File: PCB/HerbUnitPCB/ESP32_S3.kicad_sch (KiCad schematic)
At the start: 26 parts, among them J1 USB_C_Receptacle_USB2.0_16P, J2 Barrel_Jack_Switch_Pin3Ring, SW1 SW_Push, SW2 SW_Push, U1 USBLC6-2P6, U2 ESP32-S3-WROOM-1, U3 AMS1117-5.0, U4 AP2112K-3.3

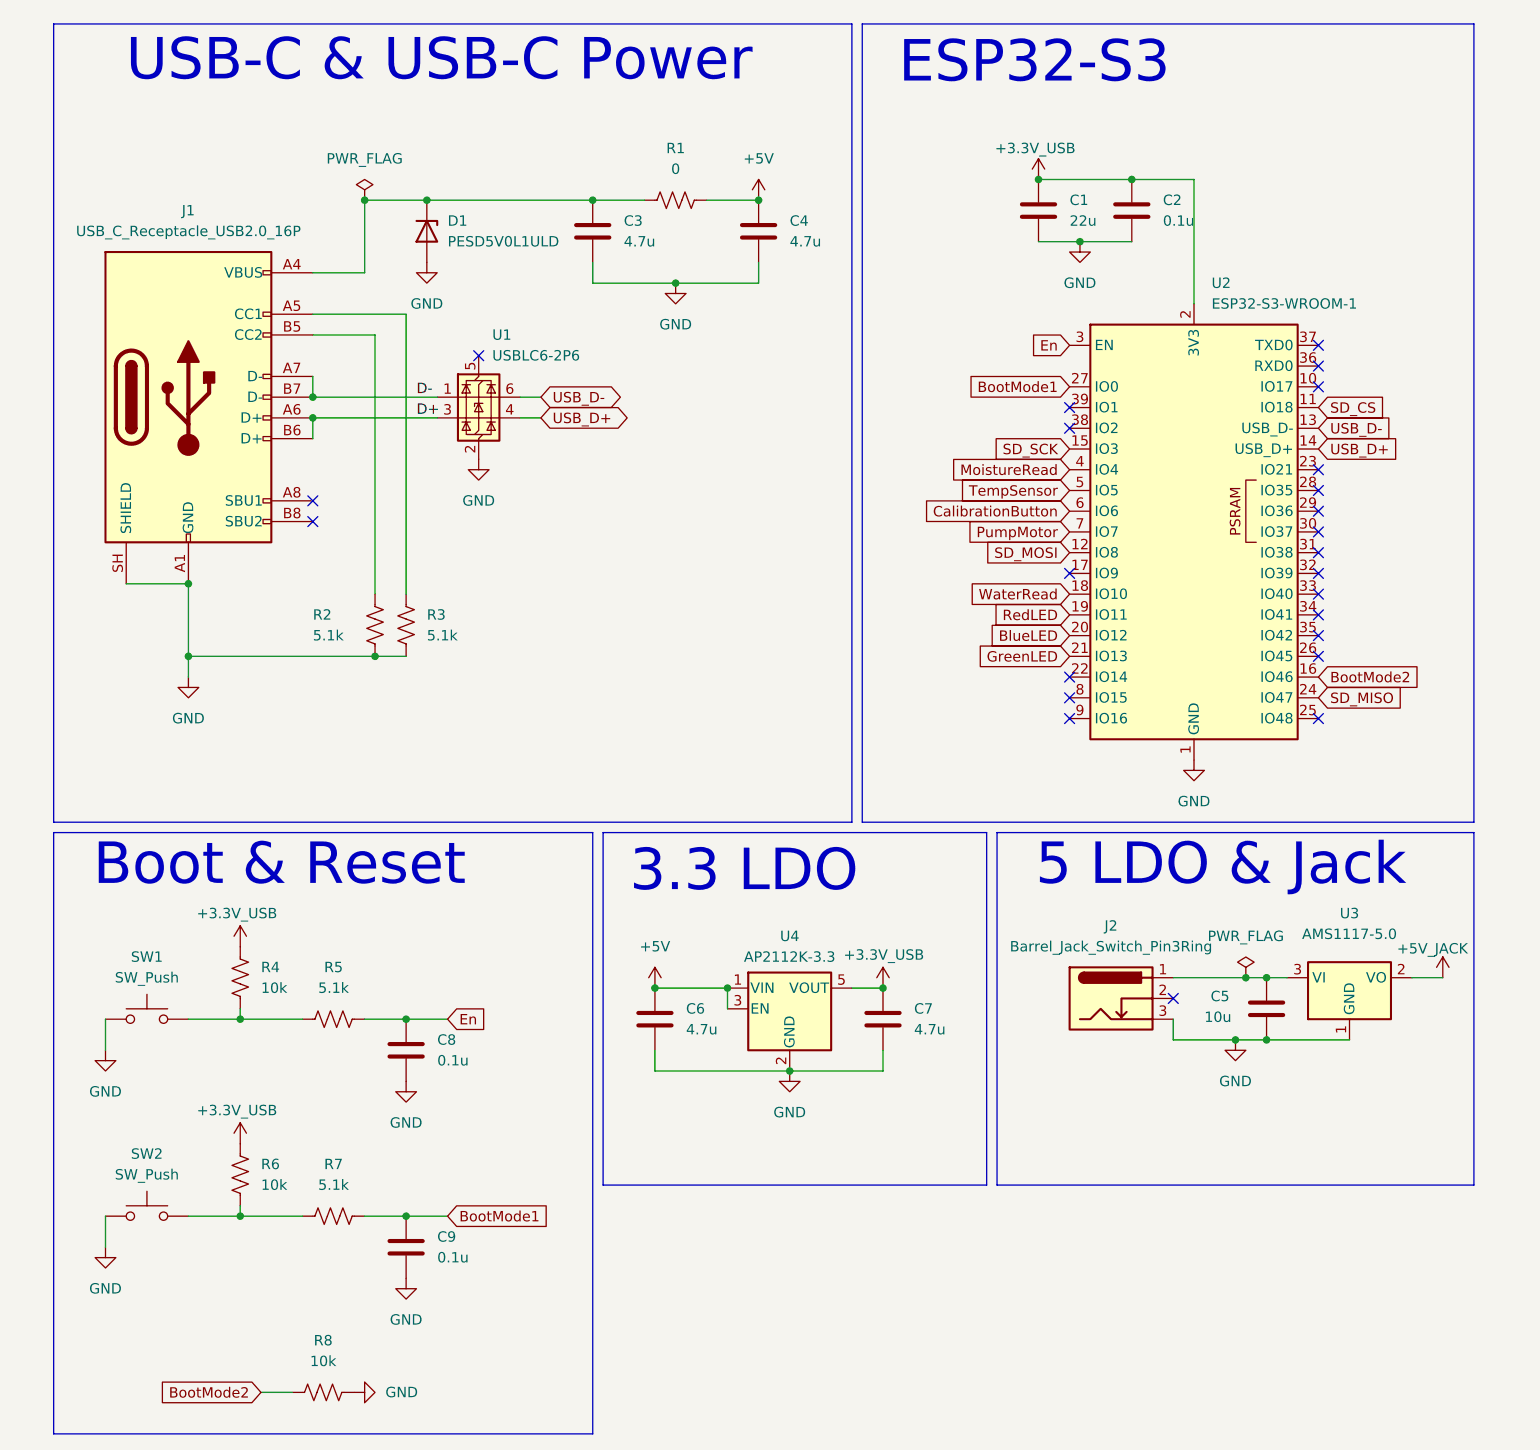
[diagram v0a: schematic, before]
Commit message: Started PCB design
- Assigned footprints to remaining components
- Brought components into PCB editor and laid them out in general groups
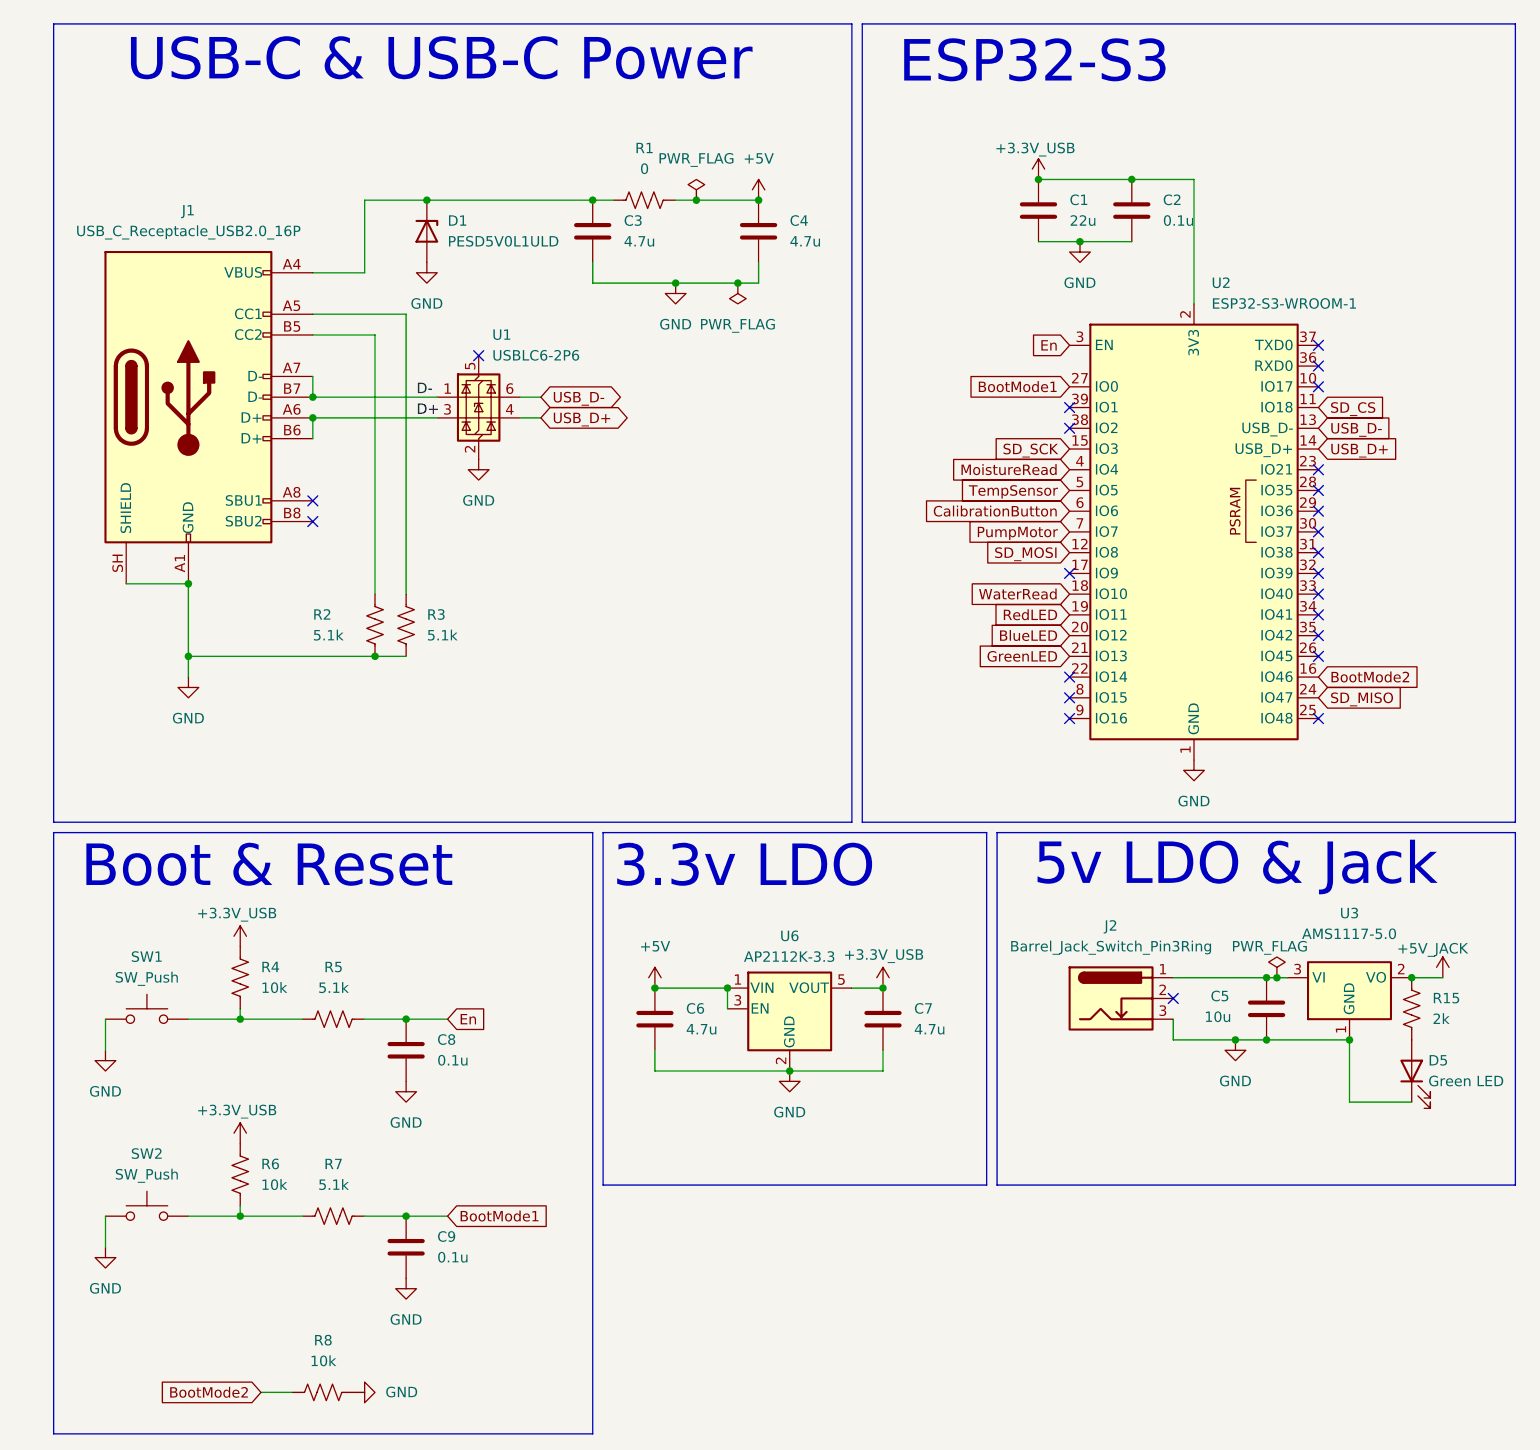
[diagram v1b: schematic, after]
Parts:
- removed U4: AP2112K-3.3, Package_TO_SOT_SMD:SOT-23-5, symbol Regulator_Linear:AP2112K-3.3
- added D5: Green LED, LED_SMD:LED_0201_0603Metric, symbol Device:LED
- added R15: 2k, Resistor_SMD:R_0402_1005Metric, symbol Device:R_US
- added U6: AP2112K-3.3, Package_TO_SOT_SMD:SOT-23-5, symbol Regulator_Linear:AP2112K-3.3
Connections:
- net +3.3V_USB: now also U6.5 (VOUT)
- net +5V: now also U6.1 (VIN), U6.3 (EN)
- net +5V_JACK: now also R15.1
- net GND: now also D5.1 (K), U6.2 (GND)
- new net: D5.2 (A), R15.2
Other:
- note added: "3.3v LDO"
- note added: "5v LDO & Jack"
- note removed: "3.3 LDO"
- note removed: "5 LDO & Jack"
- moved on the sheet: R1

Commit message: Arranged components
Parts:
- C1, C3, C4, C5, C6, C7: footprint Capacitor_SMD:C_0402_1005Metric -> Capacitor_SMD:C_0805_2012Metric
- R1: footprint (none) -> Resistor_SMD:R_0805_2012Metric
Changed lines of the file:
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@@
 			)
 		)
-		(property "Footprint" "Capacitor_SMD:C_0402_1005Metric"
+		(property "Footprint" "Capacitor_SMD:C_0805_2012Metric"
 			(at 116.5352 139.7 0)
 			(hide yes)
@@
 			)
 		)
-		(property "Footprint" "Capacitor_SMD:C_0402_1005Metric"
+		(property "Footprint" "Capacitor_SMD:C_0805_2012Metric"
 			(at 80.9752 43.18 0)
 			(hide yes)
@@
 			)
 		)
-		(property "Footprint" "Capacitor_SMD:C_0402_1005Metric"
+		(property "Footprint" "Capacitor_SMD:C_0805_2012Metric"
 			(at 88.5952 139.7 0)
 			(hide yes)
@@
 			)
 		)
-		(property "Footprint" "Capacitor_SMD:C_0402_1005Metric"
+		(property "Footprint" "Capacitor_SMD:C_0805_2012Metric"
 			(at 163.5252 138.43 0)
 			(hide yes)
@@
 			)
 		)
-		(property "Footprint" ""
+		(property "Footprint" "Resistor_SMD:R_0805_2012Metric"
 			(at 86.614 34.544 90)
 			(hide yes)
@@
 			)
 		)
-		(property "Footprint" "Capacitor_SMD:C_0402_1005Metric"
+		(property "Footprint" "Capacitor_SMD:C_0805_2012Metric"
 			(at 101.2952 43.18 0)
 			(hide yes)
@@
 			)
 		)
-		(property "Footprint" "Capacitor_SMD:C_0402_1005Metric"
+		(property "Footprint" "Capacitor_SMD:C_0805_2012Metric"
 			(at 135.5852 40.64 0)
 			(hide yes)
